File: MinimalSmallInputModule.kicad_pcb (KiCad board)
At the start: 2 copper layers, 33.8 x 131 mm, 18 parts, among them J1 Pogo Pins, J2 Debug Header

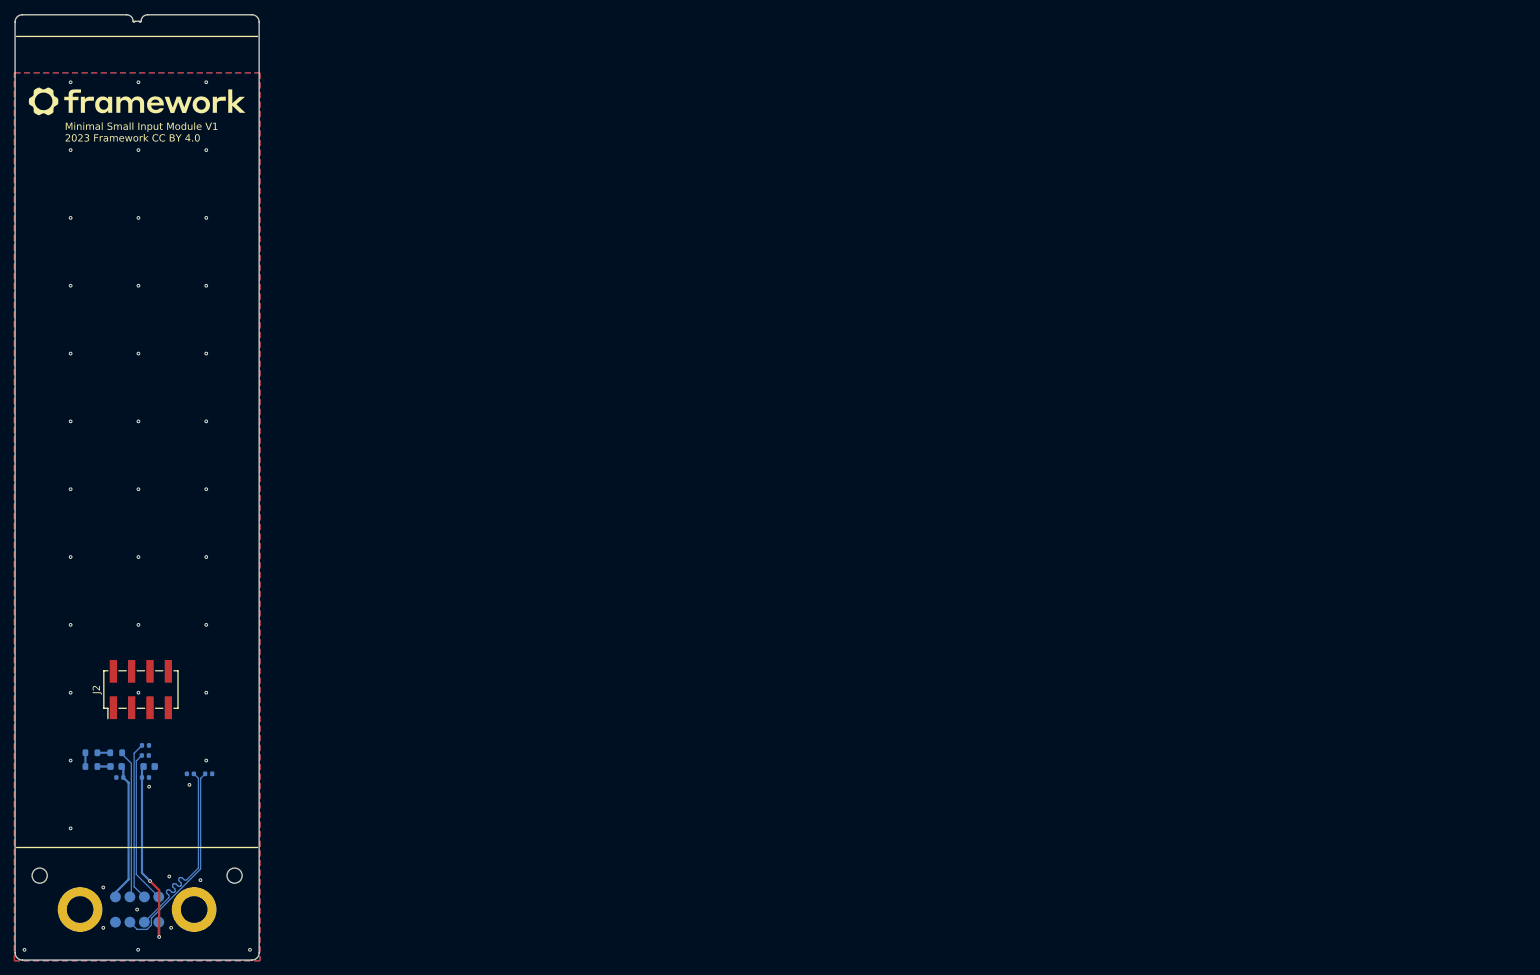
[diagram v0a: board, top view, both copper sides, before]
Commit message: First complete version sent to JLCPCB
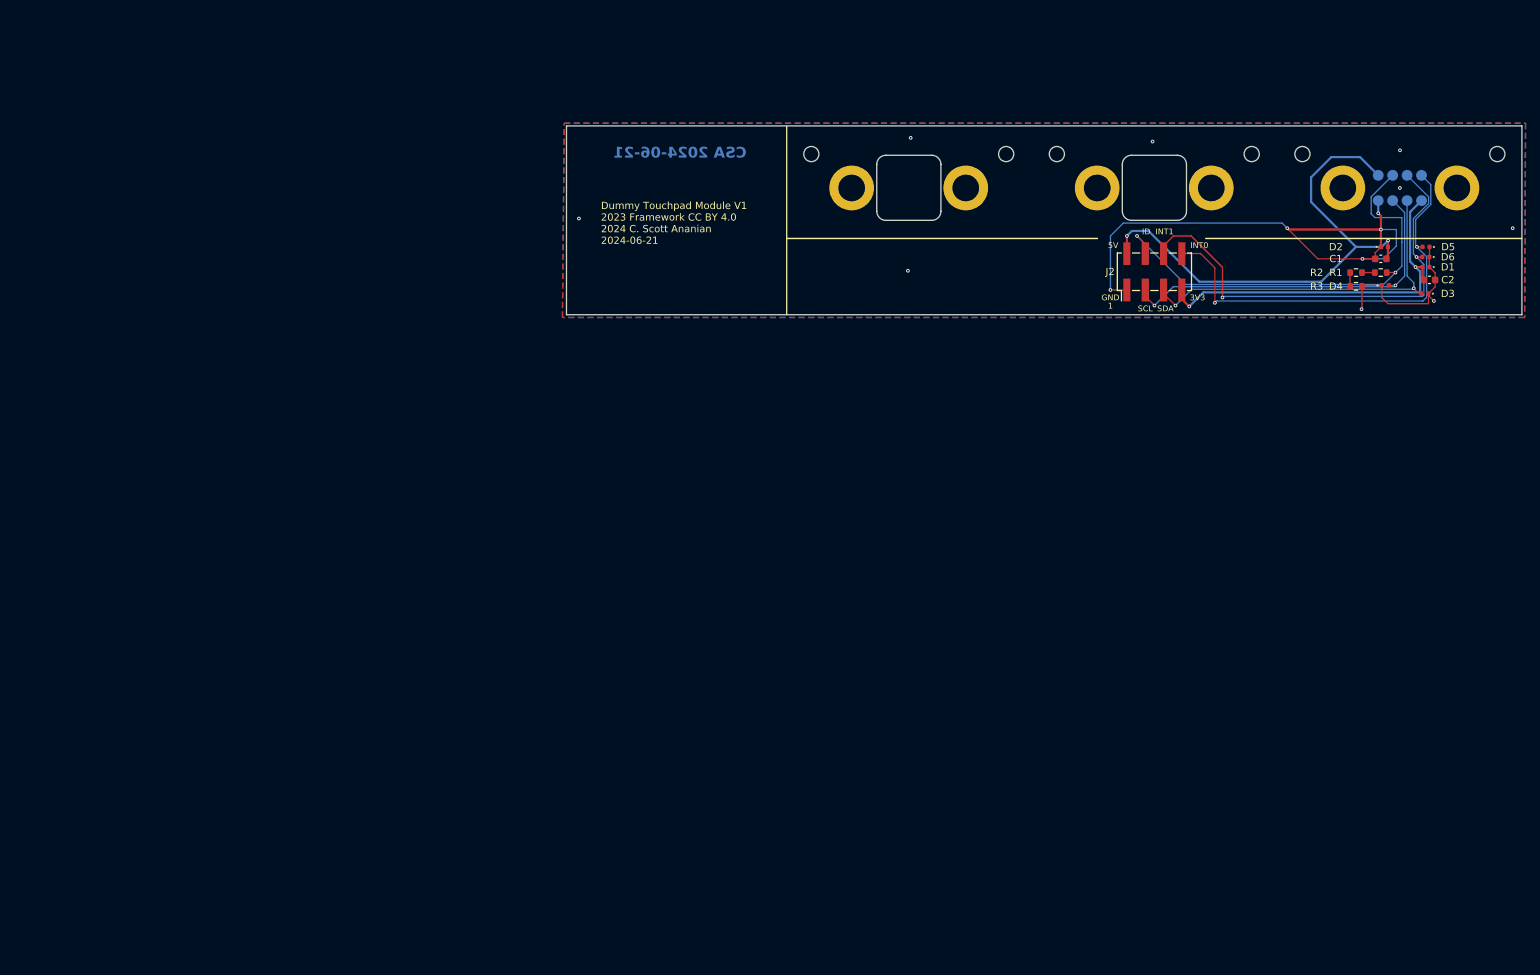
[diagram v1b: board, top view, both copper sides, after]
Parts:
- removed G***: LOGO, InputModule:Framework-Logo_3.8mm_SilkScreen
- added H1: 24929, InputModule:MountingHole_3.7mm_Pad_24929, B.Cu at (165.9, 74.0)
- added H2: 24929, InputModule:MountingHole_3.7mm_Pad_24929, B.Cu at (181.8, 74.0)
- added H3: MountingHole, MountingHole:MountingHole_2.1mm, F.Cu at (160.3, 69.3)
- added H4: MountingHole, MountingHole:MountingHole_2.1mm, F.Cu at (187.3, 69.3)
- added H5: 24929, InputModule:MountingHole_3.7mm_Pad_24929, B.Cu at (200.0, 74.0)
- added H6: 24929, InputModule:MountingHole_3.7mm_Pad_24929, B.Cu at (215.8, 74.0)
- added H7: MountingHole, MountingHole:MountingHole_2.1mm, F.Cu at (194.4, 69.3)
- added H8: MountingHole, MountingHole:MountingHole_2.1mm, F.Cu at (221.4, 69.3)
- C1, C2, D1, D2, D3, D4, D5, D6, R1, R2, R3: moved to F.Cu
- moved H10 201.6 mm to (249.8, 74.0)
- moved H11 201.6 mm to (228.4, 69.3)
- moved H12 201.6 mm to (255.4, 69.3)
- moved H9 201.6 mm to (234.0, 74.0)
- moved J1 201.6 mm to (241.9, 74.0)
- moved D1 191.0 mm to (245.5, 85.0)
- moved D5 191.0 mm to (245.5, 82.2)
- moved D2 190.1 mm to (239.8, 82.2)
- moved D6 189.9 mm to (245.5, 83.6)
- moved C2 189.8 mm to (246.0, 86.7)
- moved C1 188.9 mm to (239.3, 83.8)
- moved R1 187.5 mm to (239.3, 85.7)
- moved R2 187.5 mm to (235.8, 85.7)
- moved R3 187.5 mm to (235.8, 87.6)
- moved D3 183.6 mm to (245.4, 88.6), turned to 180 degrees
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- renumbered H2 to H10, H3 to H11, H4 to H12, H1 to H9
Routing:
- net GND: track 1.82 -> 105.2 mm, vias 44 -> 14
- net +5V: track 19.2 -> 70.6 mm, vias 0 -> 2
- net /BOARD_ID: track 20.1 -> 62.4 mm, vias 0 -> 2
- net /TP_INT_1: track 22.0 -> 63.9 mm, vias 0 -> 2
- net /TP_INT_0: track 21.8 -> 59.6 mm, vias 0 -> 2
- net +3V3: track 26.8 -> 52.3 mm
- net /I2C_SCL: track 27.7 -> 51.1 mm, vias 0 -> 2
- net /I2C_SDA: track 27.5 -> 50.8 mm, vias 0 -> 2
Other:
- board size 33.8 x 131 mm -> 132.4 x 26.2 mm
- board text added: "1"
- board text added: "3V3"
- board text added: "5V"
- board text added: "CSA 2024-06-21"
- board text added: "Dummy Touchpad Module V1 2023 Framework CC BY 4.0 2024 C. Scott Ananian 2024-06-21"
- board text added: "GND"
- board text added: "ID"
- board text added: "INT0"
- board text added: "INT1"
- board text added: "SCL"
- board text added: "SDA"
- board text removed: "Minimal Small Input Module V1 2023 Framework CC BY 4.0"

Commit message: Add JLCJLCJLCJLC text (not yet used)
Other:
- board text added: "JLCJLCJLCJLC"
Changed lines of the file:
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@@
 		(tags "diode")
 		(property "Reference" "D5"
-			(at -3.071 0 360)
+			(at -3.071 0 0)
 			(layer "F.SilkS")
 			(effects
@@
 		)
 		(property "Value" "D_TVS"
-			(at 0 1.17 360)
+			(at 0 1.17 0)
 			(layer "F.Fab")
 			(hide yes)
@@
 		)
 		(property "Footprint" "Diode_SMD:D_0402_1005Metric"
-			(at 0 0 360)
+			(at 0 0 0)
 			(layer "B.Fab")
 			(hide yes)
@@
 		)
 		(property "Datasheet" ""
-			(at 0 0 360)
+			(at 0 0 0)
 			(layer "B.Fab")
 			(hide yes)
@@
 		)
 		(property "Description" "Bidirectional transient-voltage-suppression diode"
-			(at 0 0 360)
+			(at 0 0 0)
 			(layer "B.Fab")
 			(hide yes)
@@
 		)
 		(fp_text user "${REFERENCE}"
-			(at 0 0 360)
+			(at 0 0 0)
 			(layer "F.Fab")
 			(effects
@@
 		(tags "resistor")
 		(property "Reference" "R1"
-			(at 6.223 0 360)
+			(at 6.223 0 0)
 			(layer "F.SilkS")
 			(effects
@@
 		)
 		(property "Value" "330k"
-			(at 0 1.43 360)
+			(at 0 1.43 0)
 			(layer "F.Fab")
 			(effects
@@
 		)
 		(fp_text user "${REFERENCE}"
-			(at 0 0 360)
+			(at 0 0 0)
 			(layer "F.Fab")
 			(effects
@@
 		(tags "capacitor")
 		(property "Reference" "C1"
-			(at 6.223 0 360)
+			(at 6.223 0 0)
 			(layer "F.SilkS")
 			(effects
@@
 		)
 		(property "Value" "10uF"
-			(at 0 1.43 360)
+			(at 0 1.43 0)
 			(layer "F.Fab")
 			(effects
@@
 		)
 		(property "Footprint" "Capacitor_SMD:C_0603_1608Metric"
-			(at 0 0 360)
+			(at 0 0 0)
 			(layer "B.Fab")
 			(hide yes)
@@
 		)
 		(property "Datasheet" ""
-			(at 0 0 360)
+			(at 0 0 0)
 			(layer "B.Fab")
 			(hide yes)
@@
 		)
 		(property "Description" "Unpolarized capacitor"
-			(at 0 0 360)
+			(at 0 0 0)
 			(layer "B.Fab")
 			(hide yes)
@@
 		)
 		(fp_text user "${REFERENCE}"
-			(at 0 0 360)
+			(at 0 0 0)
 			(layer "F.Fab")
 			(effects
@@
 		(tags "diode")
 		(property "Reference" "D1"
-			(at -3.048 0 360)
+			(at -3.048 0 0)
 			(layer "F.SilkS")
 			(effects
@@
 		)
 		(property "Value" "D_TVS"
-			(at 0 1.17 360)
+			(at 0 1.17 0)
 			(layer "F.Fab")
 			(effects
@@
 		)
 		(property "Footprint" "Diode_SMD:D_0402_1005Metric"
-			(at 0 0 360)
+			(at 0 0 0)
 			(layer "B.Fab")
 			(hide yes)
@@
 		)
 		(property "Datasheet" ""
-			(at 0 0 360)
+			(at 0 0 0)
 			(layer "B.Fab")
 			(hide yes)
@@
 		)
 		(property "Description" "Bidirectional transient-voltage-suppression diode"
-			(at 0 0 360)
+			(at 0 0 0)
 			(layer "B.Fab")
 			(hide yes)
@@
 		)
 		(fp_text user "${REFERENCE}"
-			(at 0 0 360)
+			(at 0 0 0)
 			(layer "F.Fab")
 			(effects
@@
 		(tags "resistor")
 		(property "Reference" "R2"
-			(at -5.461 0 360)
+			(at -5.461 0 0)
 			(layer "F.SilkS")
 			(effects
@@
 		)
 		(property "Value" "220k"
-			(at 0 1.43 360)
+			(at 0 1.43 0)
 			(layer "F.Fab")
 			(effects
@@
 		)
 		(fp_text user "${REFERENCE}"
-			(at 0 0 360)
+			(at 0 0 0)
 			(layer "F.Fab")
 			(effects
@@
 		(tags "capacitor")
 		(property "Reference" "C2"
-			(at 2.54 0 360)
+			(at 2.54 0 0)
 			(layer "F.SilkS")
 			(effects
@@
 		)
 		(property "Value" "10uF"
-			(at 0 1.43 360)
+			(at 0 1.43 0)
 			(layer "F.Fab")
 			(effects
@@
 		)
 		(property "Footprint" "Capacitor_SMD:C_0603_1608Metric"
-			(at 0 0 360)
+			(at 0 0 0)
 			(layer "B.Fab")
 			(hide yes)
@@
 		)
 		(property "Datasheet" ""
-			(at 0 0 360)
+			(at 0 0 0)
 			(layer "B.Fab")
 			(hide yes)
@@
 		)
 		(property "Description" "Unpolarized capacitor"
-			(at 0 0 360)
+			(at 0 0 0)
 			(layer "B.Fab")
 			(hide yes)
@@
 		)
 		(fp_text user "${REFERENCE}"
-			(at 0 0 360)
+			(at 0 0 0)
 			(layer "F.Fab")
 			(effects
@@
 		(tags "resistor")
 		(property "Reference" "R3"
-			(at 5.461 0 360)
+			(at 5.461 0 0)
 			(layer "F.SilkS")
 			(effects
@@
 		)
 		(property "Value" "10k"
-			(at 0 1.43 360)
+			(at 0 1.43 0)
 			(layer "F.Fab")
 			(effects
@@
 		)
 		(fp_text user "${REFERENCE}"
-			(at 0 0 360)
+			(at 0 0 0)
 			(layer "F.Fab")
 			(effects
@@
 		(tags "diode")
 		(property "Reference" "D6"
-			(at -3.048 0 360)
+			(at -3.048 0 0)
 			(layer "F.SilkS")
 			(effects
@@
 		)
 		(property "Value" "D_TVS"
-			(at 0 1.17 360)
+			(at 0 1.17 0)
 			(layer "F.Fab")
 			(effects
@@
 		)
 		(fp_text user "${REFERENCE}"
-			(at 0 0 360)
+			(at 0 0 0)
 			(layer "F.Fab")
 			(effects
@@
 		)
 		(property "Footprint" "Diode_SMD:D_0402_1005Metric"
-			(at 0 0 360)
+			(at 0 0 0)
 			(layer "B.Fab")
 			(hide yes)
@@
 		)
 		(property "Datasheet" ""
-			(at 0 0 360)
+			(at 0 0 0)
 			(layer "B.Fab")
 			(hide yes)
@@
 		)
 		(property "Description" "Bidirectional transient-voltage-suppression diode"
-			(at 0 0 360)
+			(at 0 0 0)
 			(layer "B.Fab")
 			(hide yes)
@@
 		(tags "diode")
 		(property "Reference" "D2"
-			(at -6.731 0 360)
+			(at -6.731 0 0)
 			(layer "F.SilkS")
 			(effects
@@
 		)
 		(property "Value" "D_TVS"
-			(at 0 1.17 360)
+			(at 0 1.17 0)
 			(layer "F.Fab")
 			(effects
@@
 		)
 		(property "Footprint" "Diode_SMD:D_0402_1005Metric"
-			(at 0 0 360)
+			(at 0 0 0)
 			(layer "B.Fab")
 			(hide yes)
@@
 		)
 		(property "Datasheet" ""
-			(at 0 0 360)
+			(at 0 0 0)
 			(layer "B.Fab")
 			(hide yes)
@@
 		)
 		(property "Description" "Bidirectional transient-voltage-suppression diode"
-			(at 0 0 360)
+			(at 0 0 0)
 			(layer "B.Fab")
 			(hide yes)
@@
 		)
 		(fp_text user "${REFERENCE}"
-			(at 0 0 360)
+			(at 0 0 0)
 			(layer "F.Fab")
 			(effects
@@
 			)
 			(justify left bottom mirror)
+		)
+	)
+	(gr_text "JLCJLCJLCJLC"
+		(at 151.003 87.249 0)
+		(layer "B.SilkS")
+		(effects
+			(font
+				(size 1.5 1.5)
+				(thickness 0.15)
+			)
+			(justify left bottom mirror)
